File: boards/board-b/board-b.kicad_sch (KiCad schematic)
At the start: 65 parts, among them J10 2541WR-2X08P, J11 2541WR-2X08P, J5 B6B-XH-A(LF)(SN), J6 63951-1, J7 63951-1, J8 63951-1, J9 63951-1, P1 ATT/PDOK pads, U2 LM2596S-ADJ, U3 LM2596S-ADJ, U4 LM2596S-ADJ, U6 L7812CD2T, U7 L7805ABD2T, U8 CJ7912

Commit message: fix(#150): C3/C11 are a Phi 8 can, not Phi 10 — correct the land and the evidence
Issue #150 framed this as a layout-time decision: shrink the C3/C11 land to
Phi 8, or keep the Phi 10 pad deliberately and record why. It is neither — it
is a plain mistake. The HRK datasheet already cited by src-c2983319-datasheet
(sha256 verified unchanged) states the case three ways on page 1: the header
"GVT, 25v, 470uF, 8x10.5", the description "D8H10.5mm", and a Dimension &
Marking table giving A 8.3 / B 8.3 / C 9.0 / D 8.0 / P 3.1 / L 10.5. Those map
digit-for-digit onto CAP-SMD_BD8.0-L8.3-W8.3-LS9.0-FD, which already existed in
the library and is already used by C9.

The record carried no dimension fact at all because the bundle's retained
extract claimed in-PDF text extraction was garbled. That is true of the FOLLON
PDF (zero extractable characters) but false of this one — it extracts cleanly.

Only the 25 V line moves. EFVH035ADA471M10B0 (C22387780, the other 470 uF line
sharing the same footprint string) decodes via FOLLON's own part-number key as
diameter code 10 / height code B0 = Phi 10 x 10.5, and 470 uF/35 V is not
offered in a Phi 8 case at all, so its BD10.0 land is correct and untouched.

Also corrects two badly wrong numbers found in the same record while adding the
dimension fact. Both came from the same bad partial extraction and both ran in
the non-conservative direction:

  - ripple current: recorded ~1.0 A @120Hz/85C; datasheet says 240 mA
    @120Hz/105C, with a published x1.30 multiplier at 10kHz and above, so
    312 mA at the LM2596's 150 kHz. ~4x out.
  - ESR: recorded ~0.035 Ohm; tan-delta 0.18 implies ~0.51 Ohm. ~14x out.

That matters beyond bookkeeping: spec-architecture-review.md computed ~0.77 A
of output-cap ripple on the -13.5 V rail shared by C11||C24 and judged it
"unbounded by any retained spec" against the ~1.0 A figure. Against 312 mA, an
even split already puts C11 ~1.25x over its rating. Flagged in that doc and
raised separately — no sizing 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
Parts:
- C11, C3: footprint zudo-pd:CAP-SMD_BD10.0-L10.3-W10.3-LS11.0-FD -> zudo-pd:CAP-SMD_BD8.0-L8.3-W8.3-LS9.0-FD
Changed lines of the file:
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@@
 			)
 		)
-		(property "Footprint" "zudo-pd:CAP-SMD_BD10.0-L10.3-W10.3-LS11.0-FD"
+		(property "Footprint" "zudo-pd:CAP-SMD_BD8.0-L8.3-W8.3-LS9.0-FD"
 			(at 38.1 152.4 0)
 			(effects
@@
 			)
 		)
-		(property "Footprint" "zudo-pd:CAP-SMD_BD10.0-L10.3-W10.3-LS11.0-FD"
+		(property "Footprint" "zudo-pd:CAP-SMD_BD8.0-L8.3-W8.3-LS9.0-FD"
 			(at 444.5 152.4 0)
 			(effects

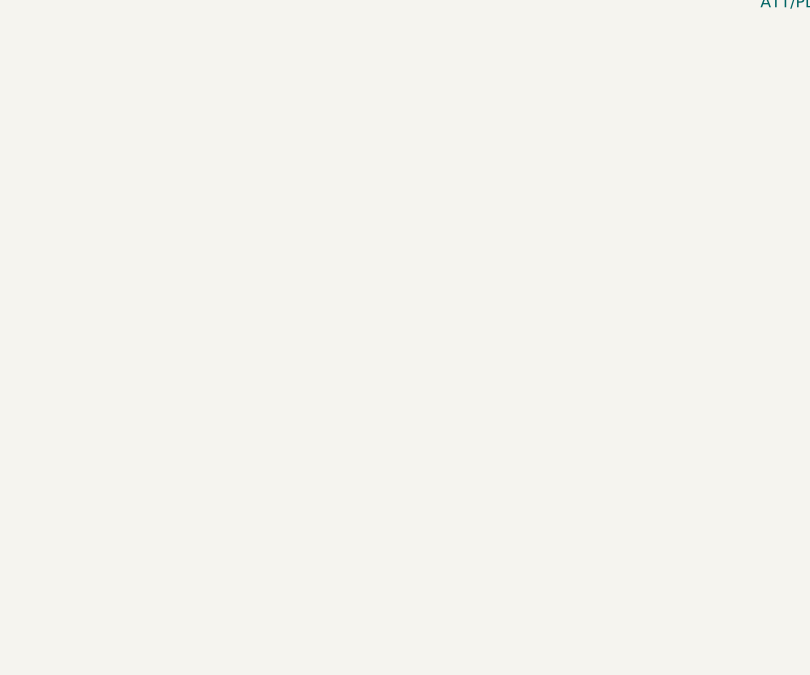
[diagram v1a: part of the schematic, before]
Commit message: fix(board-b): add C12 to -13.5V output-cap bank per locked spec (#162)
Locks decision neg-rail-cap-bank: C12 (FOLLON C22387780, 470uF/35V) is
added in parallel on the -13.5V output rail alongside C11/C24 so the
three-can bank (C11 || C24 || C12) keeps every output electrolytic
under 85% of its 150kHz-derated ripple rating at the 0.8A rated load.
C11 stays on its Phi 8 land, unswapped.

- board_b_spec.py: new C12 COMPONENTS entry + NETS pin additions
- decisions.json: locked neg-rail-cap-bank decision entry
- board-b-allow.json: C12 added_pins + _sources
- component-project-passives: two new ripple-share facts, updated
  stale exceedance fact, manifest fact-ID parity, coverage.json reasons
- component-spec-audit inventory.json: C12 placement, fitted_placements 80->81
- regenerated boards/board-b/board-b.kicad_sch (board-a unchanged)

Co-Authored-By: Claude Fable 5 <noreply@anthropic.com>
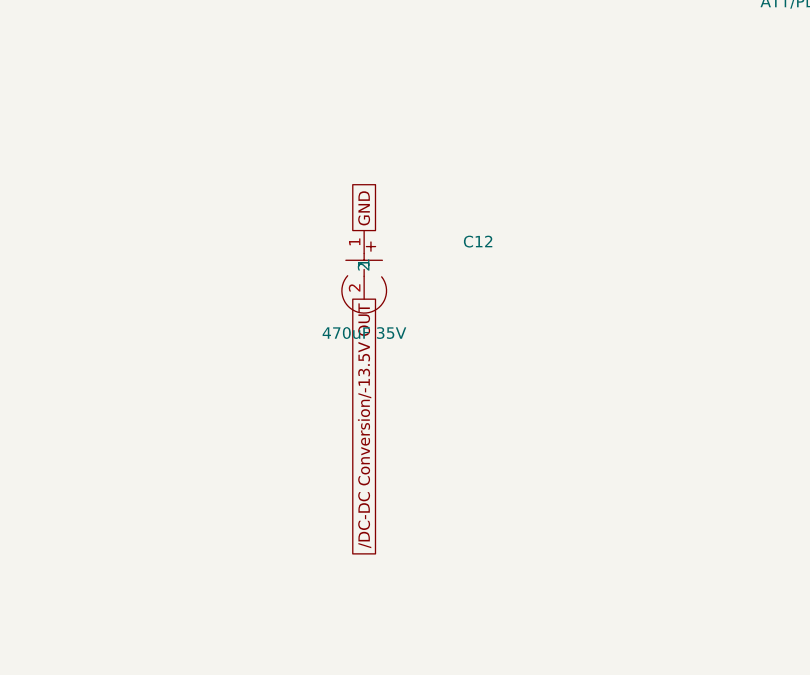
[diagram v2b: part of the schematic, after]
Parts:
- added C12: 470uF 35V, zudo-pd:CAP-SMD_BD10.0-L10.3-W10.3-LS11.0-FD, symbol zudo-pd:EFVH035ADA471M10B0
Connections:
- net /DC-DC Conversion/-13.5V OUT: now also C12.2
- net GND: now also C12.1
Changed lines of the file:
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@@
+	)
+	(symbol
+		(lib_id "zudo-pd:EFVH035ADA471M10B0")
+		(at 38.1 393.7 0)
+		(unit 1)
+		(exclude_from_sim no)
+		(in_bom yes)
+		(on_board yes)
+		(dnp no)
+		(property "Reference" "C12"
+			(at 50.8 391.16 0)
+			(effects
+				(font (size 1.27 1.27))
+			)
+		)
+		(property "Value" "470uF 35V"
+			(at 38.1 401.32 0)
+			(effects
+				(font (size 1.27 1.27))
+			)
+		)
+		(property "Footprint" "zudo-pd:CAP-SMD_BD10.0-L10.3-W10.3-LS11.0-FD"
+			(at 38.1 393.7 0)
+			(effects
+				(font (size 1.27 1.27))
+				(hide yes)
+			)
+		)
+		(property "Datasheet" ""
+			(at 38.1 393.7 0)
+			(effects
+				(font (size 1.27 1.27))
+				(hide yes)
+			)
+		)
+		(property "LCSC" "C22387780"
+			(at 38.1 401.32 0)
+			(effects
+				(font (size 1.27 1.27))
+				(hide yes)
+			)
+		)
+		(pin "1"
+		)
+		(pin "2"
+		)
+		(instances
+			(project "board-b"
+				(path "/3d627066-684f-577a-80b2-2a76742d5147"
+					(reference "C12")
+					(unit 1)
+				)
+			)
+		)
 	)
 	(symbol
@@
 		)
 	)
+	(global_label "/DC-DC Conversion/-13.5V OUT"
+		(shape passive)
+		(at 38.1 397.51 270)
+		(effects
+			(font (size 1.27 1.27))
+			(justify right)
+		)
+	)
 	(global_label "Net-(U4-Feedback)"
 		(shape passive)
@@
 		(effects
 			(font (size 1.27 1.27))
+			(justify left)
+		)
+	)
+	(global_label "GND"
+		(shape passive)
+		(at 38.1 389.89 90)
+		(effects
+			(font (size 1.27 1.27))
